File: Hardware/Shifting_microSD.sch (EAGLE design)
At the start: 21 parts, among them J1 USD_CONNECTOR, Q1 200mA/50V, Q2 200mA/50V, Q3 200mA/50V, Q4 200mA/50V, U2 3.3V

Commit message: Initial design finished
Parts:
- removed Q1, Q2, Q3, Q4: 200mA/50V, SparkFun-DiscreteSemi:MOSFET-NCHANNELBSS138
- removed R10, R11, R4, R5, R6, R7, R8, R9: 10K, SparkFun-Resistors:10KOHM-1/10W-1%(0603)0603
- added C3, C4: 0.1uF, SparkFun-Capacitors:0.1UF-25V(+80/-20%)(0603)
- added FID1, FID2, FID3, FID4: FIDUCIAL1X2, SparkFun-Aesthetics:FIDUCIAL1X2
- added LOGO1: SFE_LOGO_FLAME.3_INCH, SparkFun-Aesthetics:SFE_LOGO_FLAME.3_INCH
- added LOGO2: OSHW-LOGOS, SparkFun-Aesthetics:OSHW-LOGOS
- added U1: (no value), SparkFun-DigitalIC:TXB0104PWRSOIC14
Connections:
- removed net !CS: J1.!CS, Q4.S, R10.1
- removed net N$2: JP1.5, Q3.D, R9.1
- removed net N$5: JP1.4, Q2.D, R7.1
- removed net N$7: JP1.3, Q1.D, R5.1
- removed net SCK: J1.SCK, Q2.S, R6.1
- removed net VCC: C1.1, JP1.7, R11.2, R5.2, R7.2, R9.2, U2.EN, U2.IN
- new net !CS_3V3: J1.!CS, U1.A1
- new net 3.3V: C4.1, U1.OE, U1.VCCA
- new net DI_3V3: J1.DI, U1.A2
- new net DO_3V3: J1.DO, U1.A4
- new net N$3: JP1.4, U1.B3
- new net SCK_3V3: J1.SCK, U1.A3
- new net VDD_IO: C1.1, C3.1, JP1.7, R3.2, U1.VCCB, U2.EN, U2.IN
- net 3V3: no longer Q1.G, Q2.G, Q3.G, Q4.G, R10.2, R3.2, R4.2, R6.2, R8.2
- net DI: now also JP1.5, U1.B2; no longer J1.DI, Q3.S, R8.1
- net DO: now also JP1.3, U1.B4; no longer J1.DO, Q1.S, R4.1
- net GND: now also C3.2, C4.2, U1.GND
- net N$1: now also U1.B1; no longer Q4.D, R11.1
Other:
- note added: "+3.3V LINEAR REGULATOR"
- note added: "LEVEL TRANSLATOR PULL-UP RESISTORS"
- note added: "OE must be relative to VCCA"
- note added: "Place very close to TBX0104"
- note added: "When VCC drops below about 3.0V @ 25MHz the output wave form starts to degrade fast."
- moved on the sheet: C1, C2, J1, JP1, R1, R2, R3, U2

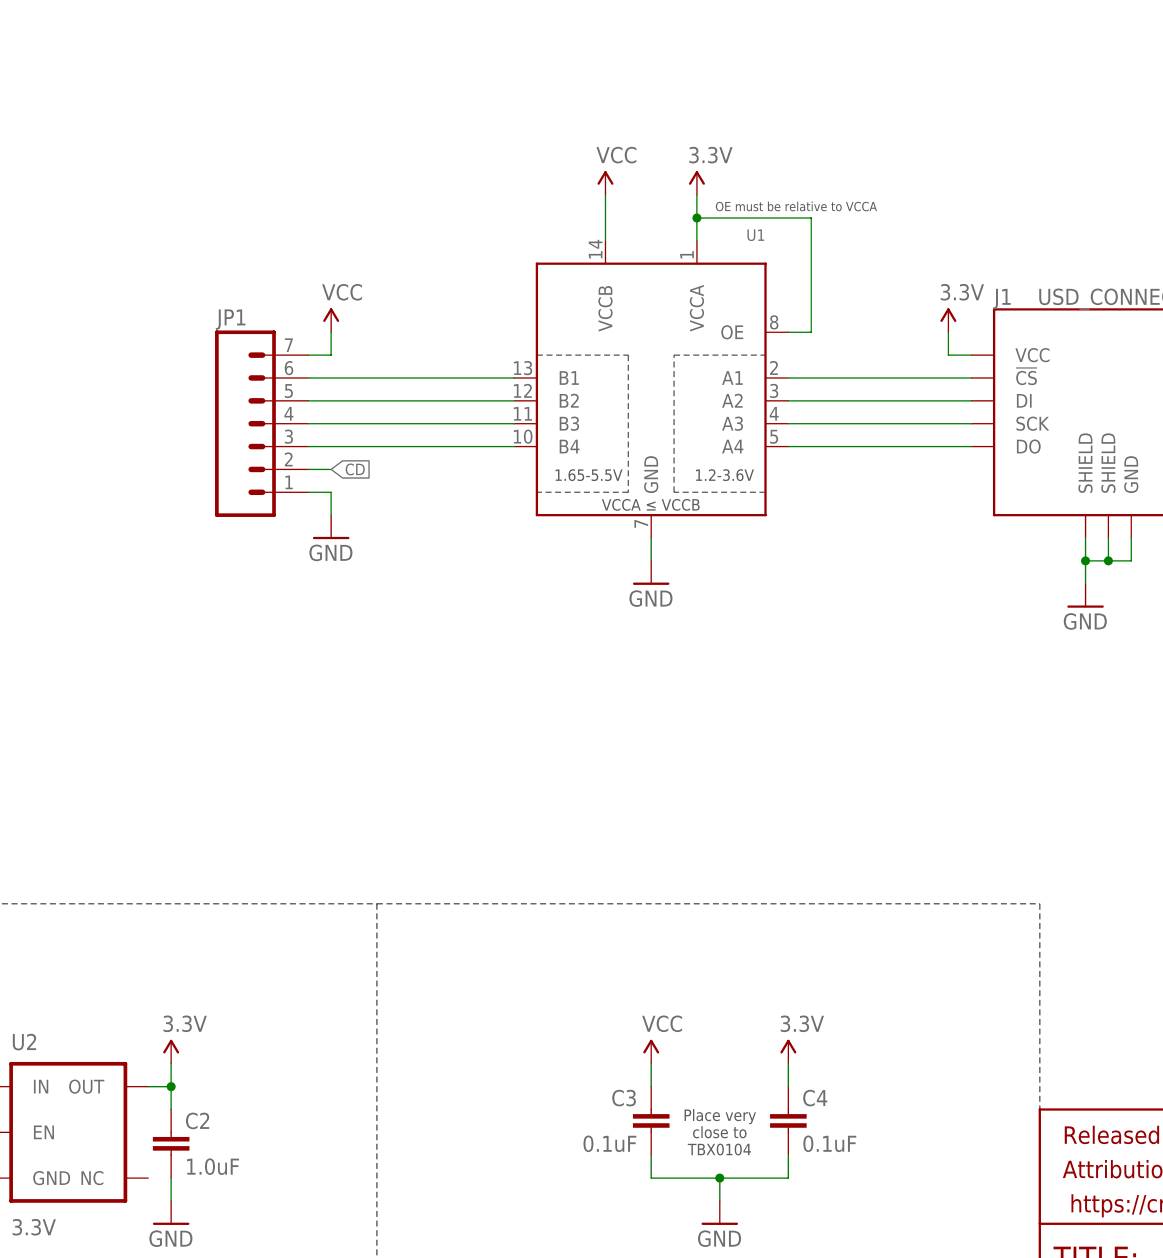
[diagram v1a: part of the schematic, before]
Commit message: Added CS pull-up
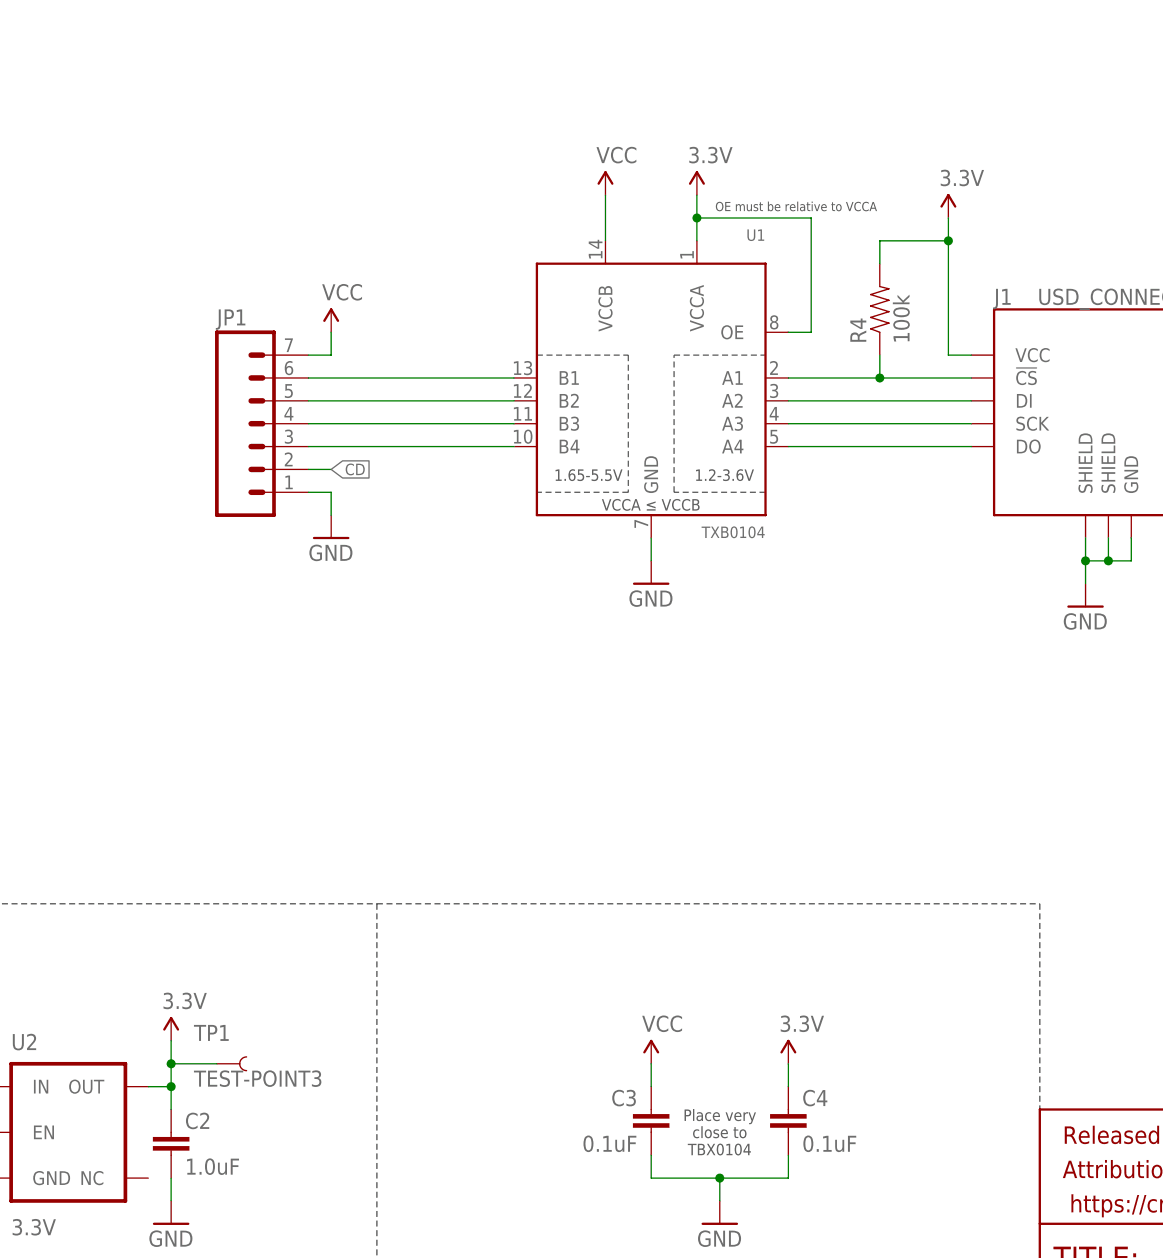
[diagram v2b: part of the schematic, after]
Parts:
- added R4: 100k, SparkFun-Resistors:100KOHM-1/10W-1%(0603)
- added TP1: TEST-POINT3, SparkFun-Passives:TEST-POINT3
- U1: value (none) -> TXB0104
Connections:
- net !CS_3V3: now also R4.1
- net 3V3: now also R4.2, TP1.1
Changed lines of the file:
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@@
 <layer number="113" name="IDFDebug" color="4" fill="1" visible="yes" active="yes"/>
 <layer number="114" name="Badge_Outline" color="11" fill="1" visible="no" active="no"/>
+<layer number="115" name="ReferenceISLANDS" color="7" fill="1" visible="yes" active="yes"/>
 <layer number="116" name="Patch_BOT" color="9" fill="4" visible="yes" active="yes"/>
 <layer number="118" name="Rect_Pads" color="7" fill="1" visible="yes" active="yes"/>
@@
 <part name="LOGO1" library="SparkFun-Aesthetics" deviceset="SFE_LOGO_FLAME" device=".3_INCH"/>
 <part name="LOGO2" library="SparkFun-Aesthetics" deviceset="OSHW-LOGO" device="S"/>
-<part name="U1" library="SparkFun-DigitalIC" deviceset="TXB0104PWR" device="SOIC14"/>
+<part name="U1" library="SparkFun-DigitalIC" deviceset="TXB0104PWR" device="SOIC14" value="TXB0104"/>
 <part name="SUPPLY14" library="SparkFun-Aesthetics" deviceset="3.3V" device=""/>
 <part name="SUPPLY15" library="SparkFun-Aesthetics" deviceset="VCC" device=""/>
@@
 <part name="FID3" library="SparkFun-Aesthetics" deviceset="FIDUCIAL" device="1X2"/>
 <part name="FID4" library="SparkFun-Aesthetics" deviceset="FIDUCIAL" device="1X2"/>
+<part name="R4" library="SparkFun-Resistors" deviceset="100KOHM-1/10W-1%(0603)" device="" value="100k"/>
+<part name="TP1" library="SparkFun-Passives" deviceset="TEST-POINT" device="3"/>
 </parts>
 <sheets>
@@
 <instance part="FRAME1" gate="V" x="147.32" y="0"/>
 <instance part="J1" gate="1" x="154.94" y="114.3"/>
-<instance part="SUPPLY2" gate="G$1" x="137.16" y="121.92"/>
+<instance part="SUPPLY2" gate="G$1" x="137.16" y="134.62"/>
 <instance part="GND3" gate="1" x="152.4" y="91.44"/>
 <instance part="R1" gate="G$1" x="180.34" y="119.38"/>
@@
 <instance part="U2" gate="G$1" x="40.64" y="33.02"/>
 <instance part="GND2" gate="1" x="27.94" y="15.24"/>
-<instance part="SUPPLY4" gate="G$1" x="50.8" y="40.64"/>
+<instance part="SUPPLY4" gate="G$1" x="50.8" y="43.18"/>
 <instance part="SUPPLY9" gate="G$1" x="25.4" y="40.64"/>
 <instance part="C1" gate="G$1" x="25.4" y="25.4" rot="MR0"/>
@@
 <instance part="FID3" gate="G$1" x="243.84" y="27.432"/>
 <instance part="FID4" gate="G$1" x="243.84" y="30.734"/>
+<instance part="R4" gate="G$1" x="129.54" y="124.46" rot="R90"/>
+<instance part="TP1" gate="G$1" x="55.88" y="40.64"/>
 </instances>
 <busses>
@@
 <pinref part="SUPPLY2" gate="G$1" pin="3.3V"/>
 <wire x1="139.7" y1="119.38" x2="137.16" y2="119.38" width="0.1524" layer="91"/>
-<wire x1="137.16" y1="119.38" x2="137.16" y2="121.92" width="0.1524" layer="91"/>
+<wire x1="137.16" y1="119.38" x2="137.16" y2="132.08" width="0.1524" layer="91"/>
+<pinref part="R4" gate="G$1" pin="2"/>
+<wire x1="137.16" y1="132.08" x2="137.16" y2="134.62" width="0.1524" layer="91"/>
+<wire x1="129.54" y1="129.54" x2="129.54" y2="132.08" width="0.1524" layer="91"/>
+<wire x1="129.54" y1="132.08" x2="137.16" y2="132.08" width="0.1524" layer="91"/>
+<junction x="137.16" y="132.08"/>
 </segment>
 <segment>
@@
 <wire x1="50.8" y1="38.1" x2="50.8" y2="40.64" width="0.1524" layer="91"/>
 <pinref part="C2" gate="G$1" pin="1"/>
+<wire x1="50.8" y1="40.64" x2="50.8" y2="43.18" width="0.1524" layer="91"/>
 <wire x1="50.8" y1="38.1" x2="50.8" y2="35.56" width="0.1524" layer="91"/>
 <junction x="50.8" y="38.1"/>
+<pinref part="TP1" gate="G$1" pin="1"/>
+<wire x1="55.88" y1="40.64" x2="50.8" y2="40.64" width="0.1524" layer="91"/>
+<junction x="50.8" y="40.64"/>
 </segment>
 </net>
@@
 <segment>
 <pinref part="U1" gate="G$1" pin="A1"/>
-<wire x1="139.7" y1="116.84" x2="119.38" y2="116.84" width="0.1524" layer="91"/>
+<wire x1="139.7" y1="116.84" x2="129.54" y2="116.84" width="0.1524" layer="91"/>
 <pinref part="J1" gate="1" pin="!CS"/>
+<pinref part="R4" gate="G$1" pin="1"/>
+<wire x1="129.54" y1="116.84" x2="119.38" y2="116.84" width="0.1524" layer="91"/>
+<wire x1="129.54" y1="119.38" x2="129.54" y2="116.84" width="0.1524" layer="91"/>
+<junction x="129.54" y="116.84"/>
 </segment>
 </net>

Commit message: Added more notes
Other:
- note added: "100KΩ is the max Sandisk recommends"
- note added: "250mV dropout"
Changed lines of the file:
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@@
 <text x="111.76" y="10.16" size="1.778" layer="97" font="vector" ratio="15" align="center">LEVEL TRANSLATOR
 PULL-UP RESISTORS</text>
+<text x="170.18" y="128.524" size="1.016" layer="97" font="vector">100KΩ is the max Sandisk recommends</text>
+<text x="33.782" y="19.05" size="1.016" layer="97" font="vector">250mV dropout</text>
 </plain>
 <instances>

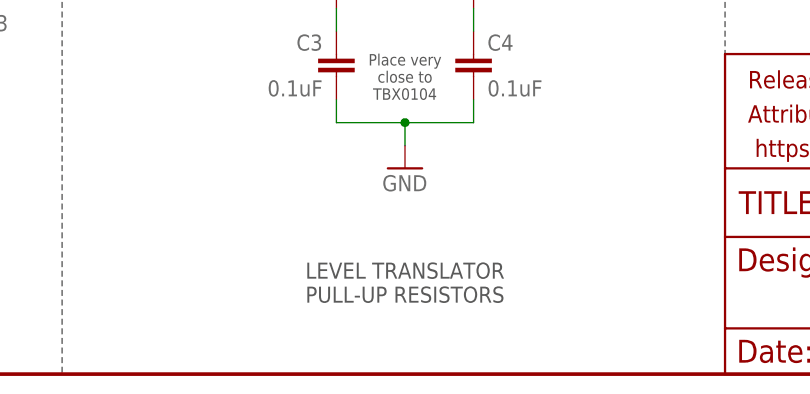
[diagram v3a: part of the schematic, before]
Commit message: Fixed copy paste error on bypass caps
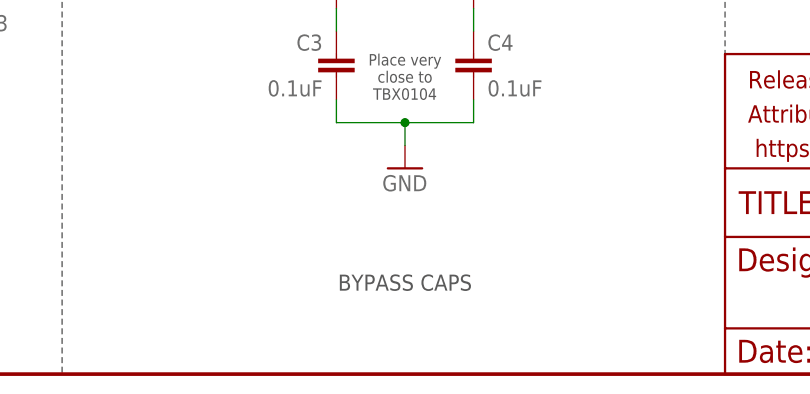
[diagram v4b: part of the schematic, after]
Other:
- note added: "BYPASS CAPS"
- note removed: "LEVEL TRANSLATOR PULL-UP RESISTORS"
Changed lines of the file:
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@@
 <wire x1="73.66" y1="58.42" x2="73.66" y2="0" width="0.1524" layer="97" style="shortdash"/>
 <text x="38.1" y="10.16" size="1.778" layer="97" font="vector" ratio="15" align="center">+3.3V LINEAR REGULATOR</text>
-<text x="111.76" y="10.16" size="1.778" layer="97" font="vector" ratio="15" align="center">LEVEL TRANSLATOR
-PULL-UP RESISTORS</text>
+<text x="111.76" y="10.16" size="1.778" layer="97" font="vector" ratio="15" align="center">BYPASS CAPS</text>
 <text x="170.18" y="128.524" size="1.016" layer="97" font="vector">100KΩ is the max Sandisk recommends</text>
 <text x="33.782" y="19.05" size="1.016" layer="97" font="vector">250mV dropout</text>

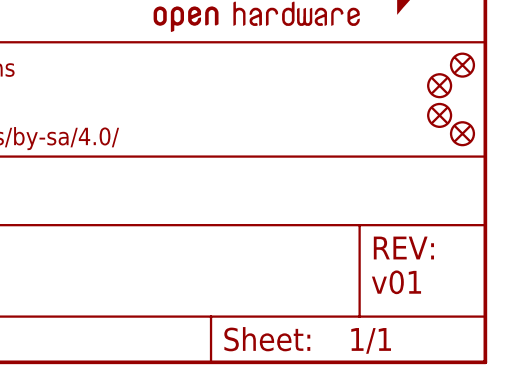
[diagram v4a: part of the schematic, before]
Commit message: Connected both 3.3V nets
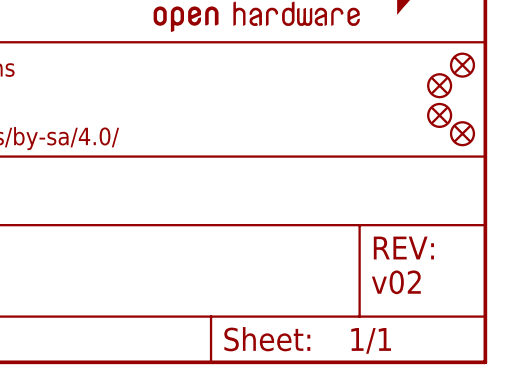
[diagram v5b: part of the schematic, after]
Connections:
- removed net 3.3V: C4.1, U1.OE, U1.VCCA
- net 3V3: now also C4.1, U1.OE, U1.VCCA
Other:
- note added: "v02"
- note removed: "v01"
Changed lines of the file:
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@@
 <plain>
 <text x="166.116" y="11.43" size="2.54" layer="94">Brent Wilkins</text>
-<text x="236.22" y="7.62" size="2.54" layer="94" font="vector">v01</text>
+<text x="236.22" y="7.62" size="2.54" layer="94" font="vector">v02</text>
 <text x="121.92" y="172.72" size="1.778" layer="97" font="vector" ratio="15" align="center">VCC +3.3V to +5.0V
 EXPECT UP TO VCC ON SIGNAL LINES</text>
@@
 <junction x="50.8" y="40.64"/>
 </segment>
+<segment>
+<pinref part="SUPPLY14" gate="G$1" pin="3.3V"/>
+<pinref part="U1" gate="G$1" pin="VCCA"/>
+<wire x1="109.22" y1="137.16" x2="109.22" y2="134.62" width="0.1524" layer="91"/>
+<pinref part="U1" gate="G$1" pin="OE"/>
+<wire x1="109.22" y1="134.62" x2="109.22" y2="132.08" width="0.1524" layer="91"/>
+<wire x1="119.38" y1="121.92" x2="121.92" y2="121.92" width="0.1524" layer="91"/>
+<wire x1="121.92" y1="121.92" x2="121.92" y2="134.62" width="0.1524" layer="91"/>
+<wire x1="121.92" y1="134.62" x2="109.22" y2="134.62" width="0.1524" layer="91"/>
+<junction x="109.22" y="134.62"/>
+</segment>
+<segment>
+<pinref part="C4" gate="G$1" pin="1"/>
+<pinref part="SUPPLY5" gate="G$1" pin="3.3V"/>
+<wire x1="119.38" y1="38.1" x2="119.38" y2="40.64" width="0.1524" layer="91"/>
+</segment>
 </net>
 <net name="!CS_3V3" class="0">
@@
 </segment>
 </net>
-<net name="3.3V" class="0">
-<segment>
-<pinref part="SUPPLY14" gate="G$1" pin="3.3V"/>
-<pinref part="U1" gate="G$1" pin="VCCA"/>
-<wire x1="109.22" y1="137.16" x2="109.22" y2="134.62" width="0.1524" layer="91"/>
-<pinref part="U1" gate="G$1" pin="OE"/>
-<wire x1="109.22" y1="134.62" x2="109.22" y2="132.08" width="0.1524" layer="91"/>
-<wire x1="119.38" y1="121.92" x2="121.92" y2="121.92" width="0.1524" layer="91"/>
-<wire x1="121.92" y1="121.92" x2="121.92" y2="134.62" width="0.1524" layer="91"/>
-<wire x1="121.92" y1="134.62" x2="109.22" y2="134.62" width="0.1524" layer="91"/>
-<junction x="109.22" y="134.62"/>
-</segment>
-<segment>
-<pinref part="C4" gate="G$1" pin="1"/>
-<pinref part="SUPPLY5" gate="G$1" pin="3.3V"/>
-<wire x1="119.38" y1="38.1" x2="119.38" y2="40.64" width="0.1524" layer="91"/>
-</segment>
-</net>

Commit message: Incremented to v10
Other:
- note added: "v10"
- note removed: "v02"
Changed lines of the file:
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@@
 <plain>
 <text x="166.116" y="11.43" size="2.54" layer="94">Brent Wilkins</text>
-<text x="236.22" y="7.62" size="2.54" layer="94" font="vector">v02</text>
+<text x="236.22" y="7.62" size="2.54" layer="94" font="vector">v10</text>
 <text x="121.92" y="172.72" size="1.778" layer="97" font="vector" ratio="15" align="center">VCC +3.3V to +5.0V
 EXPECT UP TO VCC ON SIGNAL LINES</text>
